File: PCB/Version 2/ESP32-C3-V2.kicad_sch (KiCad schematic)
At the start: 33 parts, among them J1 HCZZ0039-3, J2 DPS_PPS_Right_Angle, SW1 TS-1187A-B-A-B, SW2 TS-1187A-B-A-B, U1 USB-C-16P-SMD, U3 ESP32-C3, Y1 40MHz_S3240000151040

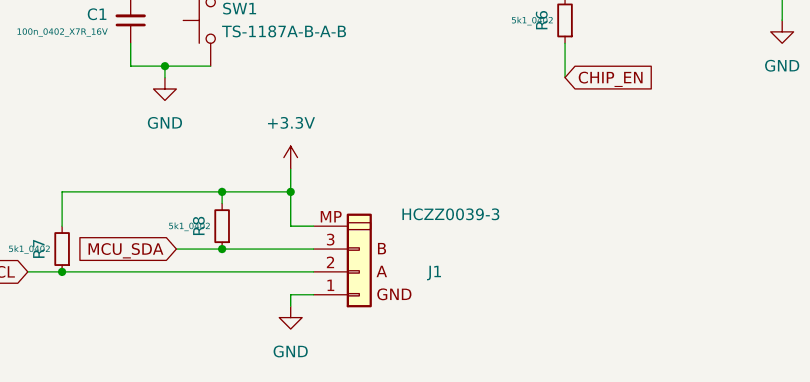
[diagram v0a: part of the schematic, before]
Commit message: changed the JST Connector to a 4 Pin
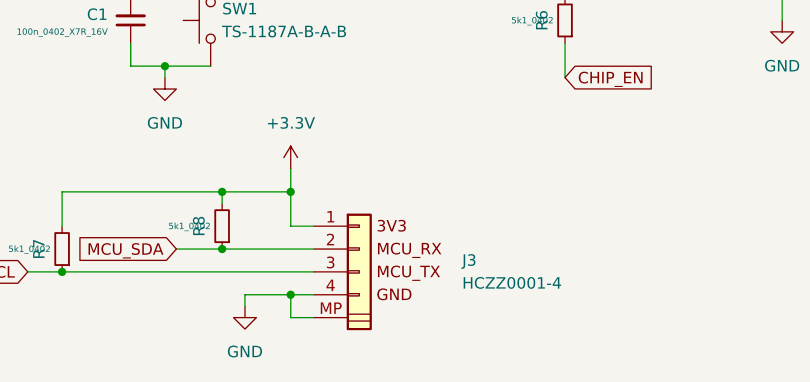
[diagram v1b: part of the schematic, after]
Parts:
- removed J1: HCZZ0039-3, Connector_JST:JST_SH_SM03B-SRSS-TB_1x03-1MP_P1.00mm_Horizontal, symbol DPS_connectors:DPS_485
- added J3: HCZZ0001-4, Connector_JST:JST_GH_SM04B-GHS-TB_1x04-1MP_P1.25mm_Horizontal, symbol DPS_connectors:DPS_UART_DEST_GH_FLAT
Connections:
- net +3.3V: now also J3.1 (Pin_1)
- net GND: now also J3.4 (Pin_4), J3.MP
- net MCU_SCL: now also J3.3 (Pin_3)
- net MCU_SDA: now also J3.2 (Pin_2)
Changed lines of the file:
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@@
 	)
 	(junction
+		(at 62.23 189.23)
+		(diameter 0)
+		(color 0 0 0 0)
+	)
+	(junction
 		(at 118.11 92.71)
 		(diameter 0)
@@
 	(wire
 		(pts
+			(xy 62.23 189.23) (xy 64.77 189.23)
+		)
+		(stroke
+			(width 0)
+			(type default)
+		)
+	)
+	(wire
+		(pts
 			(xy 54.61 184.15) (xy 64.77 184.15)
 		)
@@
 	(wire
 		(pts
+			(xy 64.77 191.77) (xy 62.23 191.77)
+		)
+		(stroke
+			(width 0)
+			(type default)
+		)
+	)
+	(wire
+		(pts
 			(xy 203.2 99.06) (xy 203.2 100.33)
 		)
@@
 	(wire
 		(pts
-			(xy 62.23 189.23) (xy 64.77 189.23)
+			(xy 57.15 189.23) (xy 62.23 189.23)
 		)
 		(stroke
@@
 	(wire
 		(pts
-			(xy 62.23 189.23) (xy 62.23 190.5)
+			(xy 57.15 189.23) (xy 57.15 190.5)
 		)
 		(stroke
@@
 	(wire
 		(pts
+			(xy 62.23 191.77) (xy 62.23 189.23)
+		)
+		(stroke
+			(width 0)
+			(type default)
+		)
+	)
+	(wire
+		(pts
 			(xy 260.35 49.53) (xy 264.16 49.53)
 		)
@@
 	)
 	(symbol
-		(lib_id "DPS_connectors:DPS_485")
-		(at 69.85 186.69 0)
-		(mirror x)
-		(unit 1)
-		(exclude_from_sim no)
-		(in_bom yes)
-		(on_board yes)
-		(dnp no)
-		(property "Reference" "J1"
-			(at 77.47 186.69 0)
-			(effects
-				(font
-					(size 1.27 1.27)
-				)
-				(justify left)
-			)
-		)
-		(property "Value" "HCZZ0039-3"
-			(at 80.01 180.34 0)
-			(effects
-				(font
-					(size 1.27 1.27)
-				)
-			)
-		)
-		(property "Footprint" "Connector_JST:JST_SH_SM03B-SRSS-TB_1x03-1MP_P1.00mm_Horizontal"
-			(at 69.215 182.245 0)
-			(effects
-				(font
-					(size 1.27 1.27)
-				)
-				(hide yes)
-			)
-		)
-		(property "Datasheet" "https://datasheet.lcsc.com/lcsc/2306261509_Hong-Cheng-HCZZ0032-3_C7433424.pdf"
-			(at 70.485 180.975 0)
-			(effects
-				(font
-					(size 1.27 1.27)
-				)
-				(hide yes)
-			)
-		)
-		(property "Description" ""
-			(at 69.85 186.69 0)
-			(effects
-				(font
-					(size 1.27 1.27)
-				)
-				(hide yes)
-			)
-		)
-		(property "LCSC" "C7433424"
-			(at 69.85 182.245 0)
-			(effects
-				(font
-					(size 1.27 1.27)
-				)
-				(hide yes)
-			)
-		)
-		(property "JLCPCB_CORRECTION" "0;0;180"
-			(at 69.85 181.61 0)
-			(effects
-				(font
-					(size 1.27 1.27)
-				)
-				(hide yes)
-			)
-		)
-		(property "Price1000" "0.0208"
-			(at 69.85 181.61 0)
-			(effects
-				(font
-					(size 1.27 1.27)
-				)
-				(hide yes)
-			)
-		)
-		(property "QtyReel" " 2000"
-			(at 69.85 180.975 0)
-			(effects
-				(font
-					(size 1.27 1.27)
-				)
-				(hide yes)
-			)
-		)
-		(pin "1"
-		)
-		(pin "2"
-		)
-		(pin "MP"
-		)
-		(pin "3"
-		)
-		(instances
-			(project "ESP32-C3"
-				(path "/35961fef-fe97-49ba-90a9-cbb988ec3bed"
-					(reference "J1")
-					(unit 1)
-				)
-			)
-		)
-	)
-	(symbol
 		(lib_id "ESP32-C3_Bib:KH-3216-H0209")
 		(at 82.55 92.71 90)
@@
 	)
 	(symbol
+		(lib_id "DPS_connectors:DPS_UART_DEST_GH_FLAT")
+		(at 69.85 184.15 0)
+		(unit 1)
+		(exclude_from_sim no)
+		(in_bom yes)
+		(on_board yes)
+		(dnp no)
+		(fields_autoplaced yes)
+		(property "Reference" "J3"
+			(at 81.28 185.4199 0)
+			(effects
+				(font
+					(size 1.27 1.27)
+				)
+				(justify left)
+			)
+		)
+		(property "Value" "HCZZ0001-4"
+			(at 81.28 187.9599 0)
+			(effects
+				(font
+					(size 1.27 1.27)
+				)
+				(justify left)
+			)
+		)
+		(property "Footprint" "Connector_JST:JST_GH_SM04B-GHS-TB_1x04-1MP_P1.25mm_Horizontal"
+			(at 68.58 179.07 0)
+			(effects
+				(font
+					(size 1.27 1.27)
+				)
+				(hide yes)
+			)
+		)
+		(property "Datasheet" "https://datasheet.lcsc.com/lcsc/2306261509_Hong-Cheng-HCZZ0001-4_C7433455.pdf"
+			(at 69.215 177.8 0)
+			(effects
+				(font
+					(size 1.27 1.27)
+				)
+				(hide yes)
+			)
+		)
+		(property "Description" "1x4P 1 GH Tinning 1.25mm Female 4 260℃ -25℃~+85℃ 1A Brass Surface Mount SMD,P=1.25mm Wire To Board / Wire To Wire Connector ROHS"
+			(at 69.85 184.15 0)
+			(effects
+				(font
+					(size 1.27 1.27)
+				)
+				(hide yes)
+			)
+		)
+		(property "LCSC" "C7433455"
+			(at 69.85 193.675 0)
+			(effects
+				(font
+					(size 1.27 1.27)
+				)
+				(hide yes)
+			)
+		)
+		(property "JLCPCB_CORRECTION" "0;0;0"
+			(at 69.85 184.15 0)
+			(effects
+				(font
+					(size 1.27 1.27)
+				)
+				(hide yes)
+			)
+		)
+		(property "Price1000" "0.0140"
+			(at 69.85 184.15 0)
+			(effects
+				(font
+					(size 1.27 1.27)
+				)
+				(hide yes)
+			)
+		)
+		(property "QtyReel" "2000"
+			(at 69.85 184.15 0)
+			(effects
+				(font
+					(size 1.27 1.27)
+				)
+				(hide yes)
+			)
+		)
+		(pin "4"
+		)
+		(pin "3"
+		)
+		(pin "MP"
+		)
+		(pin "2"
+		)
+		(pin "1"
+		)
+		(instances
+			(project ""
+				(path "/35961fef-fe97-49ba-90a9-cbb988ec3bed"
+					(reference "J3")
+					(unit 1)
+				)
+			)
+		)
+	)
+	(symbol
 		(lib_id "power:+BATT")
 		(at 74.93 31.75 0)
@@
 	(symbol
 		(lib_id "power:GND")
-		(at 62.23 190.5 0)
+		(at 57.15 190.5 0)
 		(unit 1)
 		(exclude_from_sim no)
@@
 		(fields_autoplaced yes)
 		(property "Reference" "#PWR036"
-			(at 62.23 196.85 0)
+			(at 57.15 196.85 0)
 			(effects
 				(font
@@
 		)
 		(property "Value" "GND"
-			(at 62.23 195.58 0)
+			(at 57.15 195.58 0)
 			(effects
 				(font
@@
 		)
 		(property "Footprint" ""
-			(at 62.23 190.5 0)
+			(at 57.15 190.5 0)
 			(effects
 				(font
@@
 		)
 		(property "Datasheet" ""
-			(at 62.23 190.5 0)
+			(at 57.15 190.5 0)
 			(effects
 				(font
@@
 		)
 		(property "Description" ""
-			(at 62.23 190.5 0)
+			(at 57.15 190.5 0)
 			(effects
 				(font
@@
 		)
 		(instances
-			(project "ESP32-C3"
+			(project "ESP32-C3-V2"
 				(path "/35961fef-fe97-49ba-90a9-cbb988ec3bed"
 					(page "2")

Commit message: update
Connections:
- net +BATT: now also J2.2 (Pin_2); no longer J2.1 (Pin_1)
- net GND: now also J2.1 (Pin_1); no longer J2.2 (Pin_2)
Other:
- moved on the sheet: J2
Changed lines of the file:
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@@
 	(wire
 		(pts
-			(xy 76.2 34.29) (xy 74.93 34.29)
-		)
-		(stroke
-			(width 0)
-			(type default)
-		)
-	)
-	(wire
-		(pts
 			(xy 132.08 135.89) (xy 133.35 135.89)
 		)
@@
 	(wire
 		(pts
-			(xy 74.93 31.75) (xy 74.93 34.29)
+			(xy 85.09 29.21) (xy 85.09 31.75)
 		)
 		(stroke
@@
 	(wire
 		(pts
-			(xy 74.93 36.83) (xy 76.2 36.83)
-		)
-		(stroke
-			(width 0)
-			(type default)
-		)
-	)
-	(wire
-		(pts
 			(xy 45.72 43.18) (xy 46.99 43.18)
 		)
@@
 	(wire
 		(pts
-			(xy 74.93 39.37) (xy 74.93 36.83)
+			(xy 85.09 36.83) (xy 85.09 34.29)
 		)
 		(stroke
@@
 	(symbol
 		(lib_id "power:GND")
-		(at 74.93 39.37 0)
+		(at 85.09 36.83 0)
 		(unit 1)
 		(exclude_from_sim no)
@@
 		(fields_autoplaced yes)
 		(property "Reference" "#PWR06"
-			(at 74.93 45.72 0)
+			(at 85.09 43.18 0)
 			(effects
 				(font
@@
 		)
 		(property "Value" "GND"
-			(at 74.93 44.45 0)
+			(at 85.09 41.91 0)
 			(effects
 				(font
@@
 		)
 		(property "Footprint" ""
-			(at 74.93 39.37 0)
+			(at 85.09 36.83 0)
 			(effects
 				(font
@@
 		)
 		(property "Datasheet" ""
-			(at 74.93 39.37 0)
+			(at 85.09 36.83 0)
 			(effects
 				(font
@@
 		)
 		(property "Description" ""
-			(at 74.93 39.37 0)
+			(at 85.09 36.83 0)
 			(effects
 				(font
@@
 	(symbol
 		(lib_id "DPS_connectors:DPS_PPS_Right_Angle")
-		(at 81.28 35.56 0)
+		(at 80.01 33.02 180)
 		(unit 1)
 		(exclude_from_sim no)
@@
 		(on_board yes)
 		(dnp no)
-		(fields_autoplaced yes)
 		(property "Reference" "J2"
-			(at 88.9 34.29 0)
+			(at 80.01 29.21 0)
 			(effects
 				(font
 					(size 1.27 1.27)
 				)
-				(justify left)
 			)
 		)
 		(property "Value" "DPS_PPS_Right_Angle"
-			(at 88.9 36.83 0)
+			(at 72.39 28.194 0)
 			(effects
 				(font
 					(size 1.27 1.27)
 				)
-				(justify left)
+				(hide yes)
 			)
 		)
 		(property "Footprint" "Connector_JST:JST_PH_S2B-PH-K_1x02_P2.00mm_Horizontal"
-			(at 81.28 36.83 0)
+			(at 80.01 31.75 0)
 			(effects
 				(font
@@
 		)
 		(property "Datasheet" "https://datasheet.lcsc.com/lcsc/2303231100_SHOU-HAN-2-0mm-2P-WZ_C5368738.pdf"
-			(at 81.28 36.83 0)
+			(at 80.01 31.75 0)
 			(effects
 				(font
@@
 		)
 		(property "Description" ""
-			(at 81.28 35.56 0)
+			(at 80.01 33.02 0)
 			(effects
 				(font
@@
 		)
 		(property "LCSC" "C7465576"
-			(at 81.28 36.83 0)
+			(at 80.01 31.75 0)
 			(effects
 				(font
@@
 	(symbol
 		(lib_id "power:+BATT")
-		(at 74.93 31.75 0)
+		(at 85.09 29.21 0)
 		(unit 1)
 		(exclude_from_sim no)
@@
 		(fields_autoplaced yes)
 		(property "Reference" "#PWR010"
-			(at 74.93 35.56 0)
+			(at 85.09 33.02 0)
 			(effects
 				(font
@@
 		)
 		(property "Value" "+BATT"
-			(at 74.93 26.67 0)
+			(at 85.09 24.13 0)
 			(effects
 				(font
@@
 		)
 		(property "Footprint" ""
-			(at 74.93 31.75 0)
+			(at 85.09 29.21 0)
 			(effects
 				(font
@@
 		)
 		(property "Datasheet" ""
-			(at 74.93 31.75 0)
+			(at 85.09 29.21 0)
 			(effects
 				(font
@@
 		)
 		(property "Description" ""
-			(at 74.93 31.75 0)
+			(at 85.09 29.21 0)
 			(effects
 				(font

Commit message: Working on Version 2
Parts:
- removed C12: 10n_0402_X7R_50V, Capacitor_SMD:C_0402_1005Metric, symbol capacitor_smd_standard:10n_0402_X7R_50V
- removed C14, C15: 1u_0402_X5R_25V, Capacitor_SMD:C_0402_1005Metric, symbol capacitor_smd_standard:1u_0402_X5R_25V
- removed C4: 100n_0402_X7R_16V, Capacitor_SMD:C_0402_1005Metric, symbol capacitor_smd_standard:100n_0402_X7R_16V
- removed J2: DPS_PPS_Right_Angle, Connector_JST:JST_PH_S2B-PH-K_1x02_P2.00mm_Horizontal, symbol DPS_connectors:DPS_PPS_Right_Angle
- removed L2: 2nH_0403_900mA, Resistor_SMD:R_0402_1005Metric, symbol ESP32-C3_Bib:2nH_0403_900mA
- removed R1, R6, R7, R8: 5k1_0402, Resistor_SMD:R_0402_1005Metric, symbol resistor_smd_standard:5k1_0402
- removed R12, R13, R14: 120_0402, Resistor_SMD:R_0402_1005Metric, symbol resistor_smd_standard:120_0402
- removed SW1: TS-1187A-B-A-B, switch:SW_SPST_TL3305B, symbol 1_switch:TS-1187A-B-A-B
- added C12: 100n_0402_X7R_16V, Capacitor_SMD:C_0402_1005Metric, symbol capacitor_smd_standard:100n_0402_X7R_16V
- added Q1: WPM2031-3/TR, Package_TO_SOT_SMD:SOT-723, symbol Lil-Lib:PMOS
- added R1, R19, R6: 10k_0402, Resistor_SMD:R_0402_1005Metric, symbol resistor_smd_standard:10k_0402
- added R12, R7, R8: 330_0402, Resistor_SMD:R_0402_1005Metric, symbol resistor_smd_standard:330_0402
- added R13, R14: 100k_0402, Resistor_SMD:R_0402_1005Metric, symbol resistor_smd_standard:100k_0402
- added R15: 1M_0402, Resistor_SMD:R_0402_1005Metric, symbol resistor_smd_standard:1M_0402
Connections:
- net +3.3V: now also C1.1, C7.2, U3.2 (VDD3P3), U3.3 (VDD3P3), R1.1, R19.1, R6.1; no longer J3.1 (Pin_1)
- net +BATT: now also Q1.2 (S), R15.1
- net Blau: now also R7.1
- net CHIP_EN: now also R19.2
- net EXTI: now also R1.2; no longer C1.2
- net GND: now also C1.2, R14.2; no longer C1.1
- net Grün: now also R8.1
- net Rot: now also R12.1
- net at D1.1 (RK): now also R12.2
- net at D1.3 (BK): now also R7.2
- net at D1.4 (GK): now also R8.2
- net EN_ADC: now reaches U3.12 (MTCK)
- net EN_ADC: now also C12.1
- net NCHG renamed ADC
- net ADC: now also R13.2, R14.1
- net NPGOOD: no longer names the net of U3.19 (SPIHD)
- net TD renamed GPIO8
- net GPIO8: now also R6.2
- net TMR renamed VCC_Sensor
- net VCC_Sensor: now also J3.1 (Pin_1)
- new net: C12.2, Q1.1 (G), R15.2
- new net: Q1.3 (D), R13.1
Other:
- moved on the sheet: C2, C7, D1

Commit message: Version 2
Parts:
- added C13: 100n_0402_X7R_16V, Capacitor_SMD:C_0402_1005Metric, symbol capacitor_smd_standard:100n_0402_X7R_16V
- added R5: 1k_0402, Resistor_SMD:R_0402_1005Metric, symbol resistor_smd_standard:1k_0402
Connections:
- net ADC: now also U3.18 (VDD_SPI), C13.1, R5.2; no longer R13.2, R14.1, U3.20 (SPIWP)
- net EN1: now also U3.19 (SPIHD); no longer U3.22 (SPICLK)
- net EN2: now also U3.16 (GPIO10); no longer U3.21 (SPICS0)
- net GND: now also C13.2
- net Rot: now also U3.22 (SPICLK); no longer U3.18 (VDD_SPI)
- net VCC_Sensor: now also U3.8 (GPIO3); no longer U3.16 (GPIO10)
- new net: R13.2, R14.1, R5.1
- new net TD: U3.20 (SPIWP)
- no-connect marks 16 -> 15

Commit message: V2 für Kontrolle fertig
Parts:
- added C14: 1u_0402_X5R_25V, Capacitor_SMD:C_0402_1005Metric, symbol capacitor_smd_standard:1u_0402_X5R_25V
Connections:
- net CHIP_EN: now also C14.1
- net GND: now also C14.2
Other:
- moved on the sheet: R1

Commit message: Schaltplan in als PDF
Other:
- title: (none) -> USB-ESP32-C3
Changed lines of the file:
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@@
 	(generator_version "8.0")
 	(paper "A4")
+	(title_block
+		(title "USB-ESP32-C3")
+		(date "2024-06-25")
+		(rev "V2")
+	)
 	(junction
 		(at 217.17 120.65)

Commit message: neue Bilder, Gerber, PDF
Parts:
- added R10, R9: 5k1_0402, Resistor_SMD:R_0402_1005Metric, symbol resistor_smd_standard:5k1_0402
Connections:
- net +3.3V: now also R10.1, R9.1
- net MCU_SCL: now also R10.2
- net MCU_SDA: now also R9.2

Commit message: Version 2 zur Korrektur fertig
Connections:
- net EN1: no longer names the net of U3.19 (SPIHD)
- net EN2: no longer names the net of U3.16 (GPIO10)
- net NCE: no longer names the net of U3.13 (MTDO)
- net TD: no longer names the net of U3.20 (SPIWP)
- no-connect marks 15 -> 19
